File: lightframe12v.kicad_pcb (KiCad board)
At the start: 2 copper layers, 64.8 x 38.7 mm, 53 parts, among them J1 PJ-077, J2 Conn_01x07_Female, J4 Conn_01x07_Female, J5 Conn_01x04_Female, J6 Conn_01x4_Female, Q1 MMBT2222A-TP, Q2 MMBT2222A-TP, SW1 SW_Push, SW2 SW_Push, U1 TPS562211, U2 ESP32-WROOM-32U, U3 TLC5971

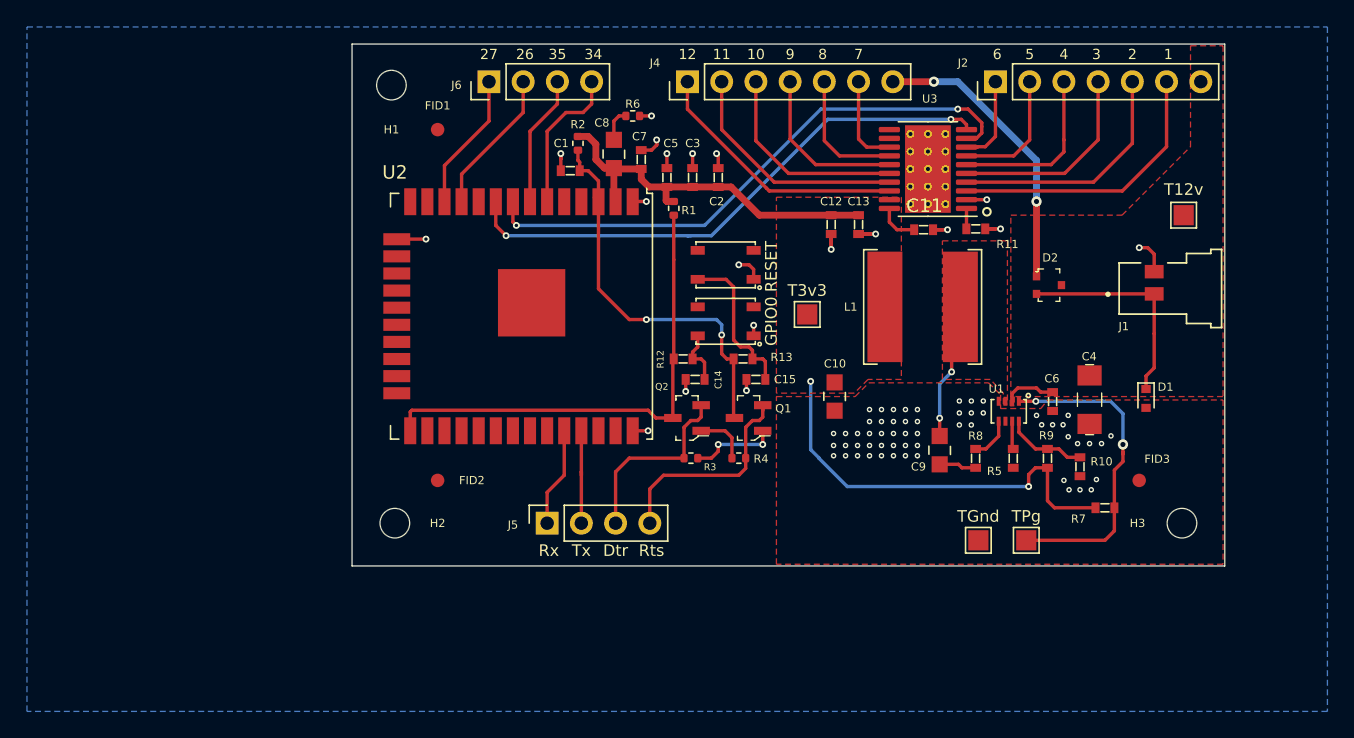
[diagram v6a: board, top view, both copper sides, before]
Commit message: changes inductor footprint.
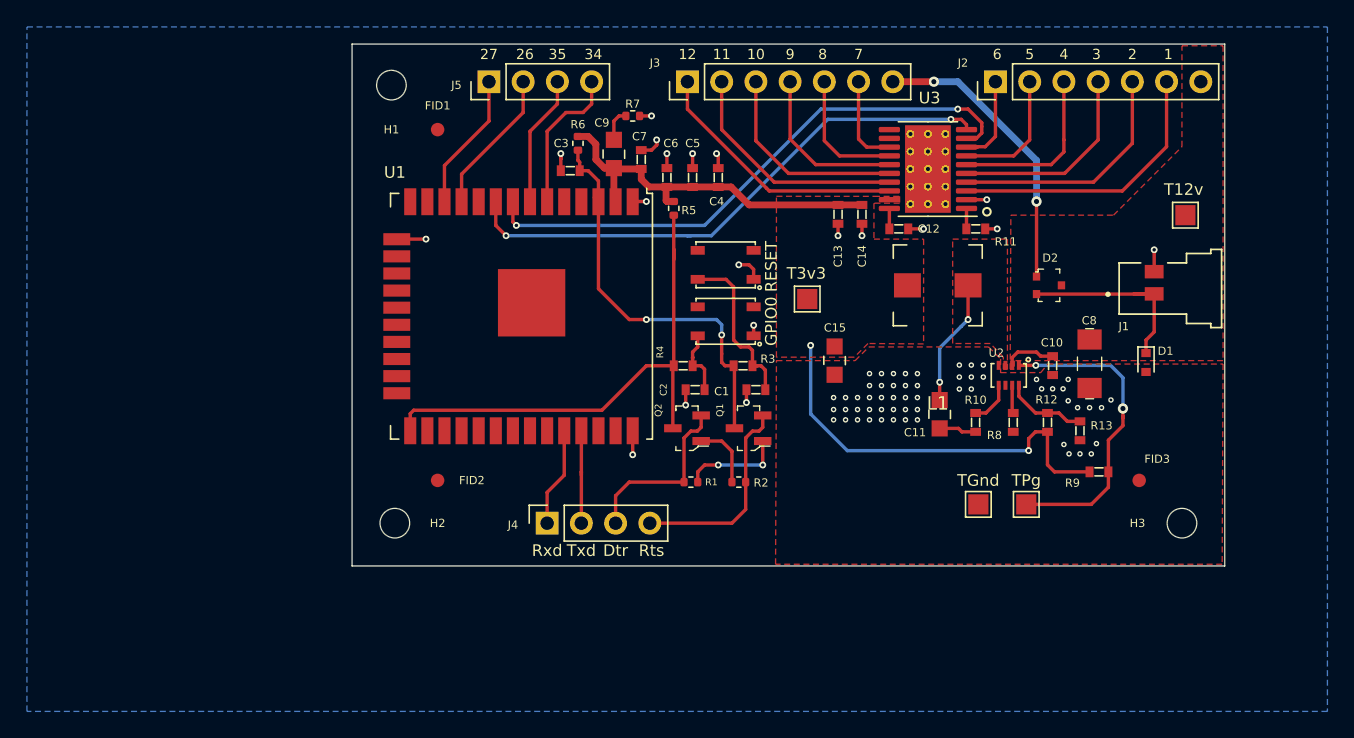
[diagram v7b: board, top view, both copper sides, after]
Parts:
- removed the C11 at (335.8, -526.0)
- added C14: 0.1uF, digikey-footprints:0603, F.Cu at (331.2, -527.1)
- C13: value 0.1uF -> 1uF
- L1: footprint Keith:SRN8040 Bournes -> Keith:SRP5030T-5R6M
- moved C12 5.03 mm to (333.9, -526.0), turned to 0 degrees
- moved R9 2.70 mm to (348.8, -508.0)
- moved C10 2.67 mm to (345.4, -515.9)
- moved C11 2.67 mm to (337.0, -512.3)
- moved C15 2.67 mm to (329.2, -516.3)
- moved C8 2.67 mm to (348.1, -516.0)
- moved R10 2.67 mm to (339.6, -511.7)
- moved R12 2.67 mm to (345.0, -511.7)
- moved R13 2.67 mm to (347.4, -511.0)
- moved R8 2.67 mm to (342.4, -511.7)
- moved TP2 2.67 mm to (343.4, -505.6)
- moved TP3 2.67 mm to (339.9, -505.6)
- moved D1 2.67 mm to (352.3, -516.1)
- moved U2 2.67 mm to (342.1, -515.2)
- moved L1 1.95 mm to (336.8, -521.8)
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- renumbered C15 to C1, C6 to C10, C9 to C11, C10 to C15, C14 to C2, C1 to C3, C2 to C4, C3 to C5, C5 to C6, C4 to C8, C8 to C9, J4 to J3, J5 to J4, J6 to J5, R3 to R1, R8 to R10, R9 to R12, R10 to R13, R4 to R2, R13 to R3, R12 to R4, R1 to R5, R2 to R6, R6 to R7, R5 to R8, R7 to R9, SW2 to SW1, SW1 to SW2, TP3 to TP2, TP2 to TP3, U2 to U1, U1 to U2
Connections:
- C12 pad 1: +3V3 -> Net-(C12-Pad1)
- U3 pad 20: Net-(C11-Pad1) (its old number) -> Net-(C12-Pad1)
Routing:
- net GND: track 28.2 -> 24.3 mm
- net Net-(C11-Pad1) (its old number): track 3.09 -> 0.00 mm
- net /Gpio0: track 36.3 -> 38.9 mm
- net Net-(D1-Pad1): track 16.2 -> 14.1 mm
- net Net-(C12-Pad1): track 0.00 -> 1.52 mm
- net Net-(C11-Pad2): track 10.6 -> 9.39 mm
- net Net-(C1-Pad2): track 11.6 -> 12.6 mm
- net Net-(Q1-Pad1): track 6.56 -> 7.57 mm
- net Net-(C2-Pad2): track 4.14 -> 5.02 mm
- net /Rts: track 16.2 -> 15.3 mm
- net Net-(Q2-Pad1): track 4.02 -> 4.89 mm
- net /Reset: track 29.6 -> 30.4 mm
- net /Dtr: track 14.1 -> 13.3 mm
- net +3V3: track 59.6 -> 58.8 mm
- net Net-(R9-Pad2): track 24.4 -> 23.8 mm
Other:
- board text added: "Rxd"
- board text added: "Txd"
- board text removed: "Rx"
- board text removed: "Tx"

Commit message: Reduced decoupling and increased traces.
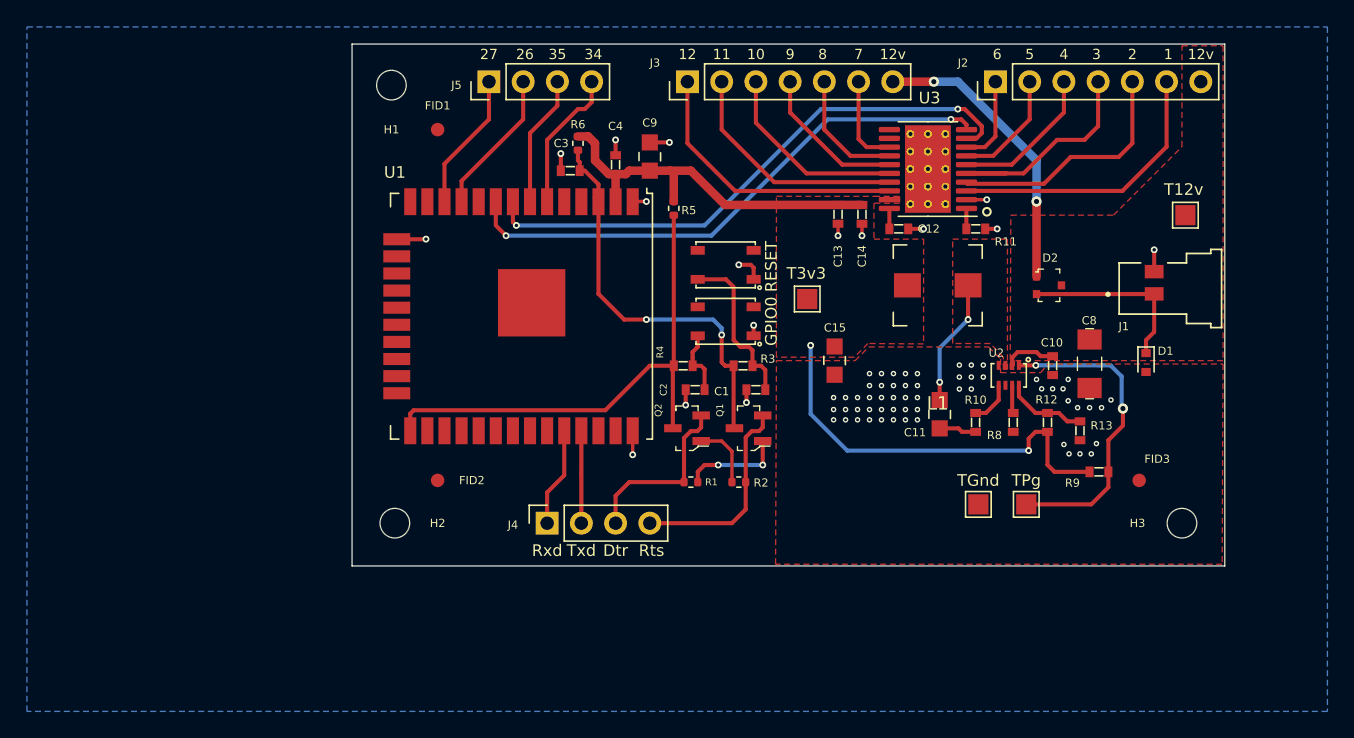
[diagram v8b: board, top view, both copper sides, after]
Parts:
- removed C5: 10000pF, digikey-footprints:0603
- removed C6: 0.1uF, digikey-footprints:0603
- removed C7: 1uF, digikey-footprints:0603
- removed R7: 1, Resistor_SMD:R_0402_1005Metric
- C4: value 0.1uF -> 0.1uF 50V (10%)
- C9: value 10uF -> 22uF 10V(20%)
- moved C4 7.68 mm to (312.9, -530.8)
- moved C9 2.67 mm to (315.5, -531.4)
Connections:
- C9 pad 2: Net-(C9-Pad2) -> GND
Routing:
- net Net-(D1-Pad1): track 14.1 -> 22.9 mm
- net /Txd: track 7.11 -> 14.0 mm
- net Net-(R9-Pad2): track 23.8 -> 30.6 mm
- net GND: track 24.3 -> 20.8 mm, vias 76 -> 73
- net +3V3: track 58.8 -> 61.8 mm
- net Net-(C9-Pad2): track 2.44 -> 0.00 mm
- net /LED3: track 15.1 -> 17.5 mm
- net /LED4: track 12.8 -> 11.1 mm
- net /LED12: track 19.5 -> 21.0 mm
- net /LED9: track 12.4 -> 11.3 mm
- net Net-(C2-Pad2): track 5.02 -> 6.04 mm
- net /LED5: track 9.50 -> 8.61 mm
- net /LED10: track 15.3 -> 14.5 mm
- net /Gpio0: track 38.9 -> 38.1 mm
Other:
- net class Default: trace_width 0.254 -> 0.3048; via_dia 0.762 -> 0.508; via_drill 0.381 -> 0.254
- board text added: "12v"
